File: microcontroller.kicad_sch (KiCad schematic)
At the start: 12 parts, among them J1 TagConnect, U1 STM32H745XIH6, U9 8132H-25.000NL33DTL

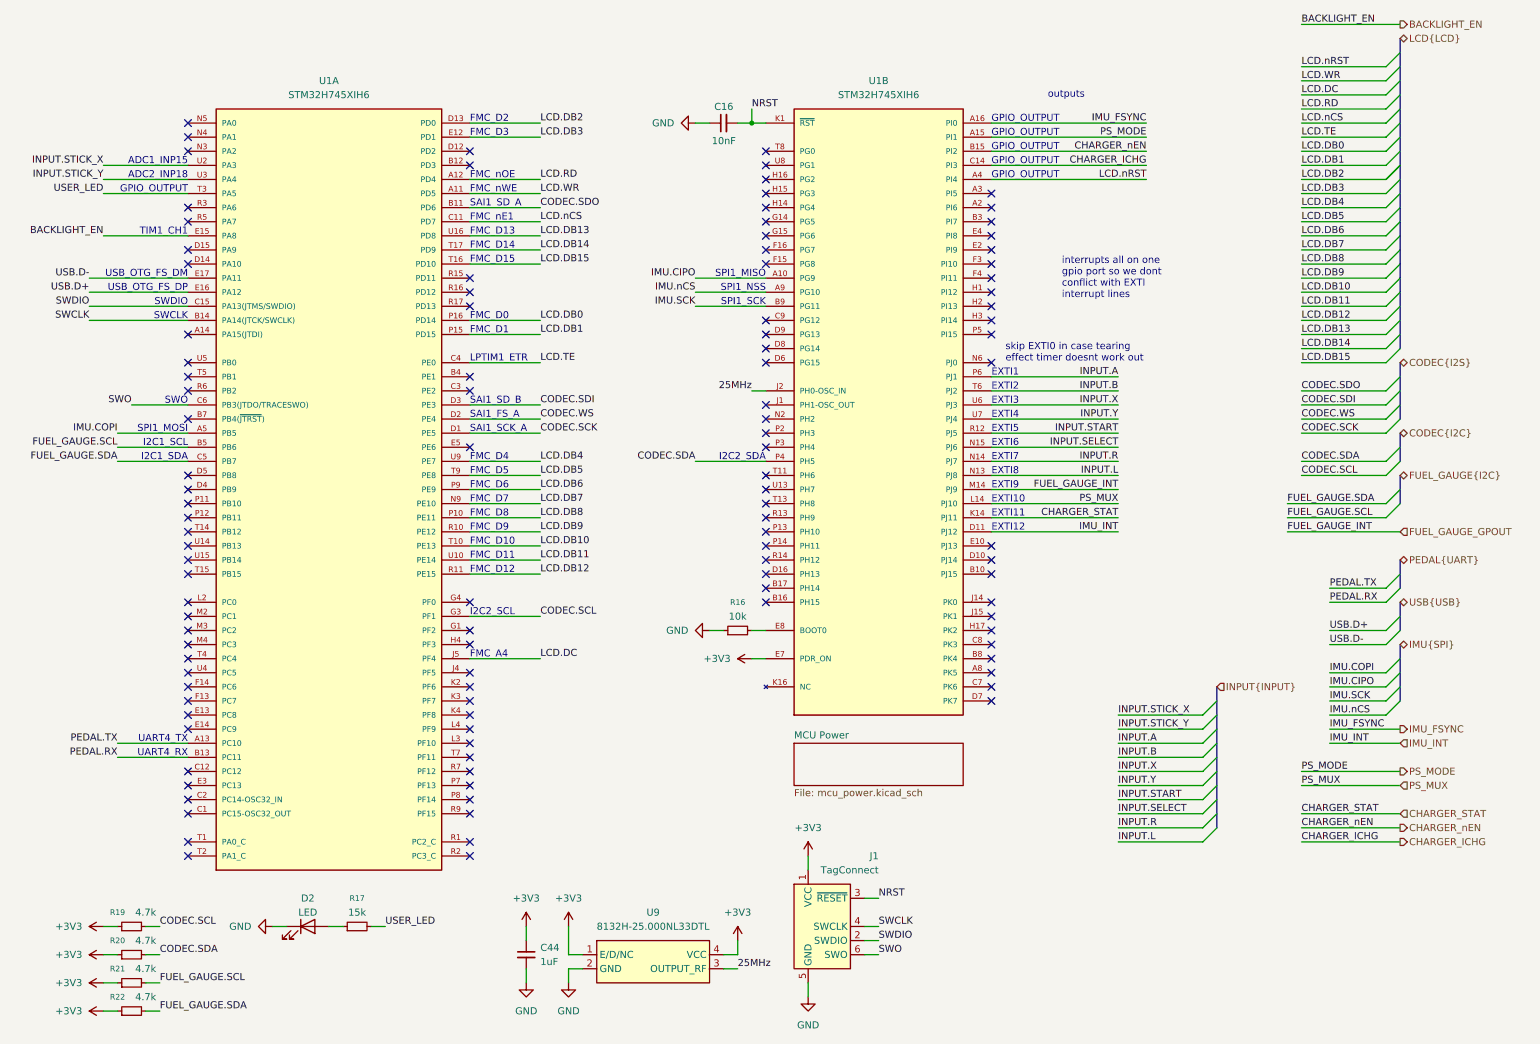
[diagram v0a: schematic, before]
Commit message: Codec (#5)
* Add codec subsheet
* Add codec ic
* Add unity gain preamp
* Finalize input buffer and filtering
* Add TPA6130A2 DirectDrive output amp
* Add in/out jacks, remove AC cap at codec input
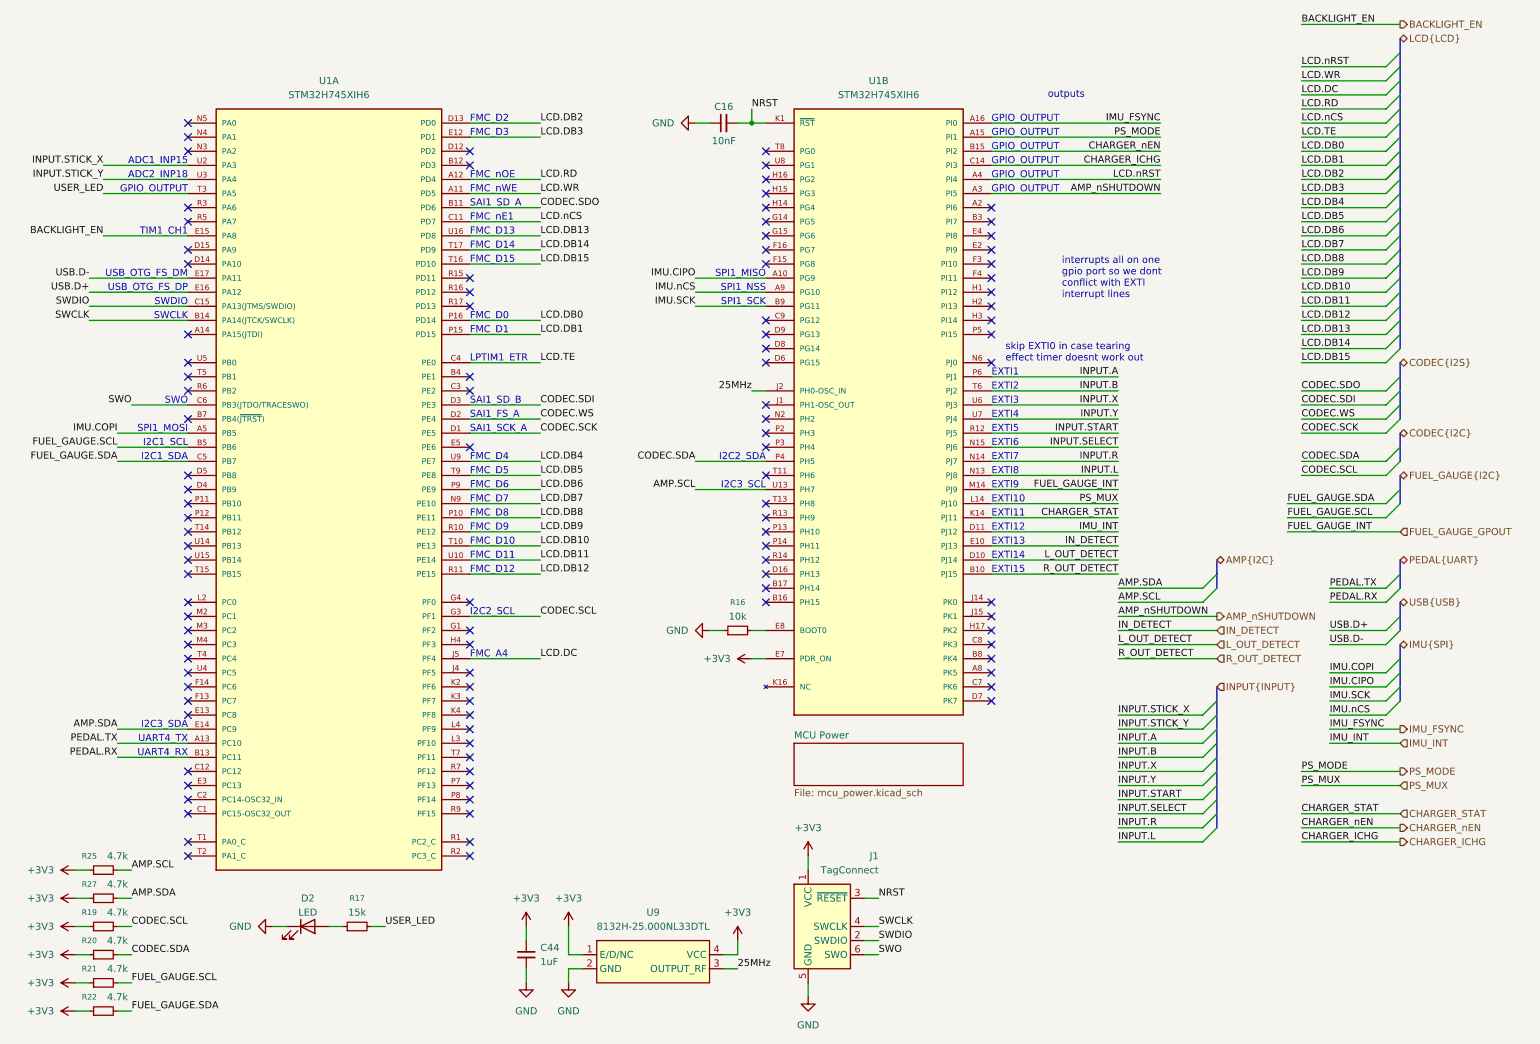
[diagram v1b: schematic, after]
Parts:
- added R25, R27: 4.7k, Resistor_SMD:R_0402_1005Metric, symbol Device:R_Small
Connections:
- net +3V3: now also R25.1, R27.1
- net AMP.SDA: now reaches U1.E14 (PC9)
- net AMP.SDA: now also R27.2
- net AMP_nSHUTDOWN: now reaches U1.A3 (PI5)
- net R_OUT_DETECT: now reaches U1.B10 (PJ15)
- net L_OUT_DETECT: now reaches U1.D10 (PJ14)
- net IN_DETECT: now reaches U1.E10 (PJ13)
- net AMP.SCL: now reaches U1.U13 (PH7)
- net AMP.SCL: now also R25.2
- no-connect marks 110 -> 104
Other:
- note added: "EXTI13"
- note added: "EXTI14"
- note added: "EXTI15"
- note added: "I2C3_SCL"
- note added: "I2C3_SDA"
- moved on the sheet: R19, R20, R21, R22
